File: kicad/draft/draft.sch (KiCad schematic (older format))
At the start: 22 parts, among them IC1 LP5024RSMR, J1 Conn_02x05_Odd_Even, U1 NodeMCU2

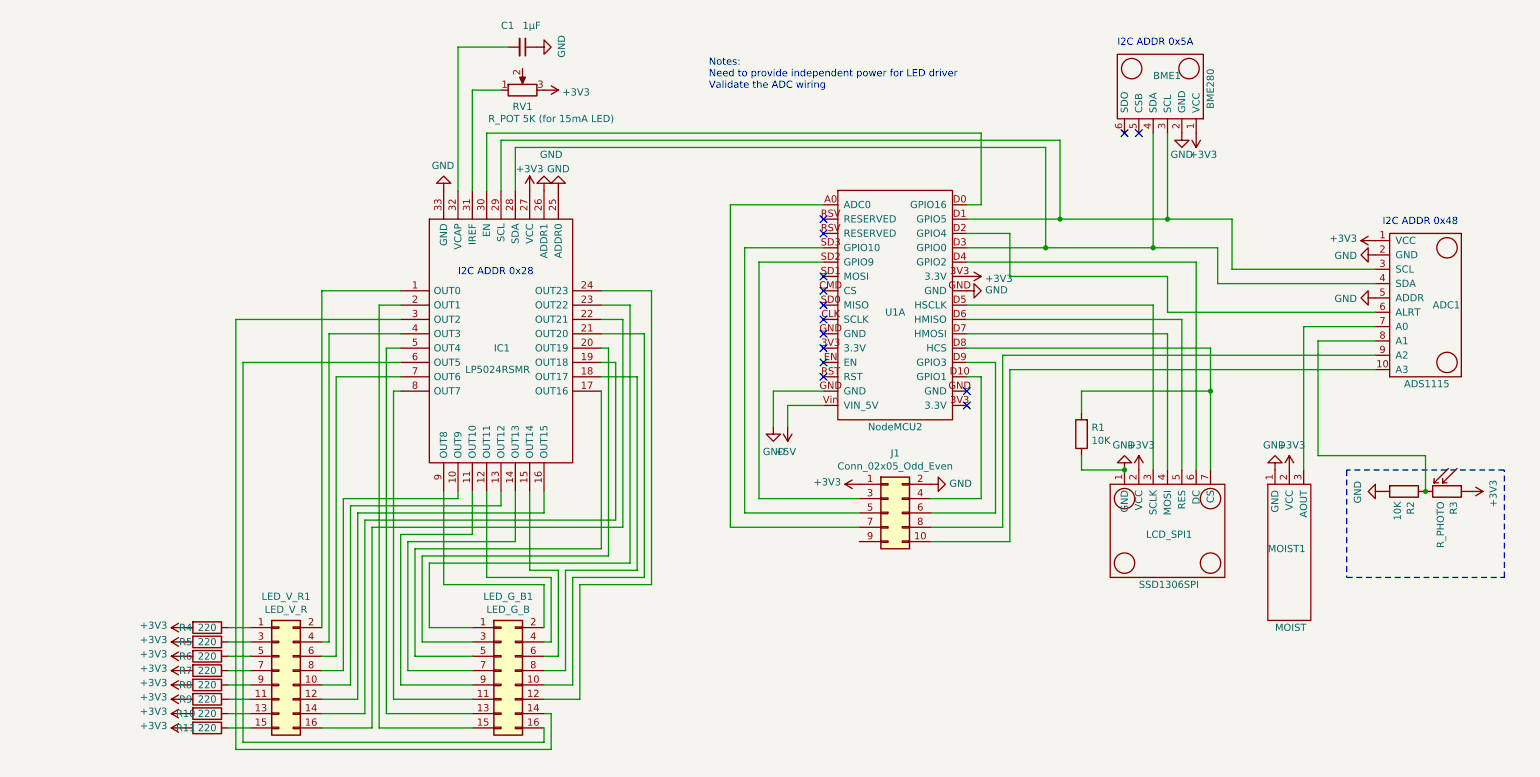
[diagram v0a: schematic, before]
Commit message: Added GND and 3V3 areas and tracks to connect NodeMCU
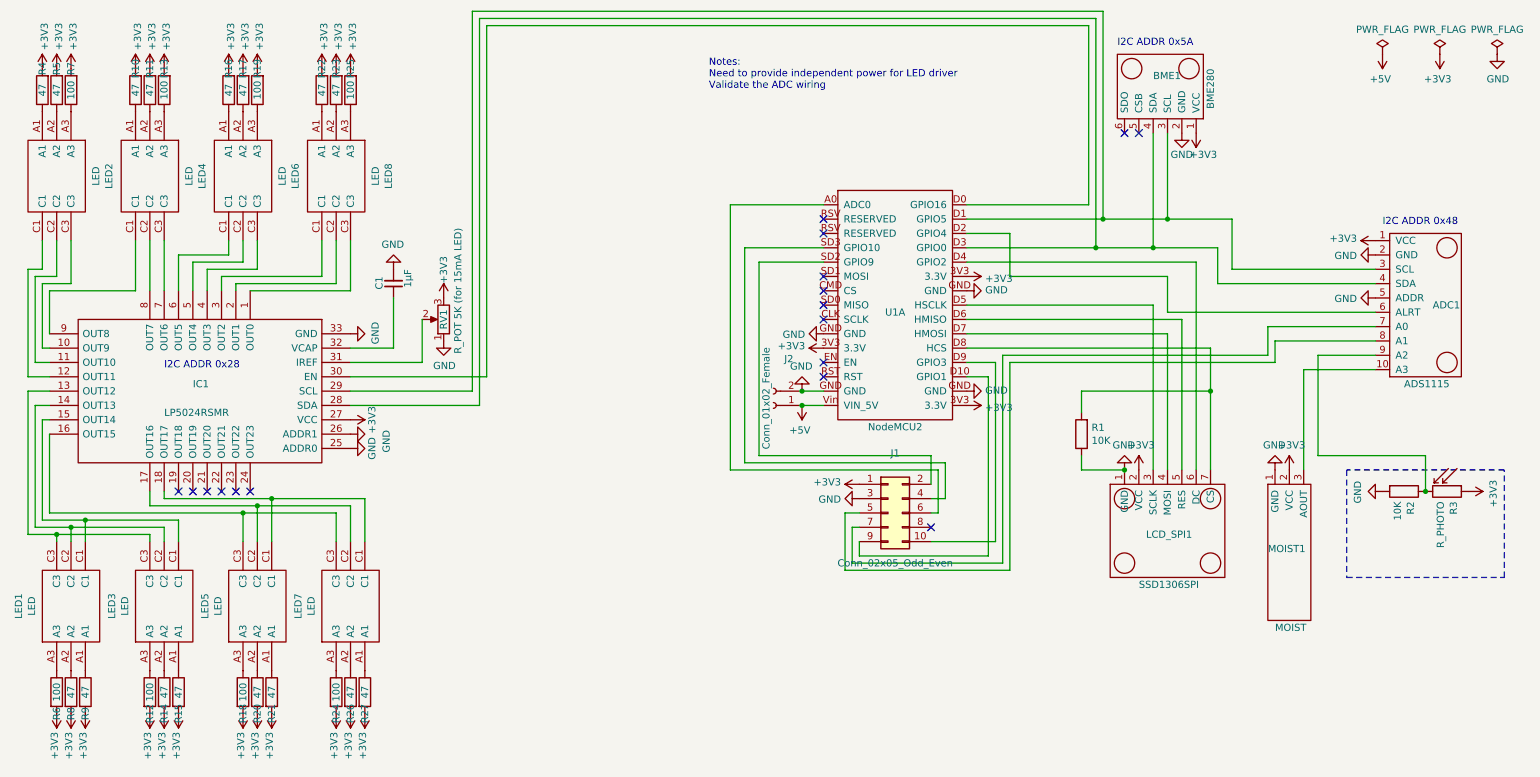
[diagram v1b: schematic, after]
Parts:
- removed LED_G_B1: LED_G_B, Connector_PinSocket_2.54mm:PinSocket_2x08_P2.54mm_Vertical, symbol Connector_Generic:Conn_02x08_Odd_Even
- removed LED_V_R1: LED_V_R, Connector_PinSocket_2.54mm:PinSocket_2x08_P2.54mm_Vertical, symbol Connector_Generic:Conn_02x08_Odd_Even
- added J2: Conn_01x02_Female, Connector_JST:JST_EH_S2B-EH_1x02_P2.50mm_Horizontal, symbol Connector:Conn_01x02_Female
- added LED1, LED2, LED3, LED4, LED5, LED6, LED7, LED8: LED, SamacSys:KRTBLSLPS132VUVXEQBTBVD8TWTZL1B, symbol SamaSys:KRTBLSLPS1.32-VUVX-EQ+BTBV-D8+TWTZ-L1-B
- added R12, R13, R18, R19, R24, R25: 100, Resistor_SMD:R_1206_3216Metric_Pad1.42x1.75mm_HandSolder, symbol Device:R
- added R14, R15, R16, R17, R20, R21, R22, R23, R26, R27: 47, Resistor_SMD:R_1206_3216Metric_Pad1.42x1.75mm_HandSolder, symbol Device:R
- R10, R11, R4, R5, R8, R9: value 220 -> 47; footprint Resistor_THT:R_Axial_DIN0207_L6.3mm_D2.5mm_P7.62mm_Horizontal -> Resistor_SMD:R_1206_3216Metric_Pad1.42x1.75mm_HandSolder
- R6, R7: value 220 -> 100; footprint Resistor_THT:R_Axial_DIN0207_L6.3mm_D2.5mm_P7.62mm_Horizontal -> Resistor_SMD:R_1206_3216Metric_Pad1.42x1.75mm_HandSolder
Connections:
- net +3V3: now also R12.2, R13.2, R14.2, R15.2, R16.2, R17.2, R18.2, R19.2, R20.2, R21.2, R22.2, R23.2, R24.2, R25.2, R26.2, R27.2
- net +5V: now also J2.1 (Pin_1)
- net GND: now also C1.2, J1.3 (Pin_3), RV1.1, J2.2 (Pin_2); no longer C1.1, J1.2 (Pin_2)
- net at U1.A0 (ADC0): now also J1.6 (Pin_6); no longer J1.7 (Pin_7)
- net at U1.D10 (GPIO1): now also J1.9 (Pin_9); no longer J1.4 (Pin_4)
- net at U1.D9 (GPIO3): now also J1.10 (Pin_10); no longer J1.6 (Pin_6)
- net at U1.SD2 (GPIO9): now also J1.2 (Pin_2); no longer J1.3 (Pin_3)
- net at U1.SD3 (GPIO10): now also J1.4 (Pin_4); no longer J1.5 (Pin_5)
- net at ADC1.10 (A3): now also MOIST1.3 (AOUT); no longer J1.10 (Pin_10)
- net at ADC1.7 (A0): now also J1.7 (Pin_7); no longer MOIST1.3 (AOUT)
- net at R2.1, R3.2: now also ADC1.9 (A2); no longer ADC1.8 (A1)
- net at J1.8 (Pin_8): no longer ADC1.9 (A2)
- net at IC1.32 (VCAP): now also C1.1; no longer C1.2
- net at IC1.8 (OUT7): now also LED4.C2
- net at IC1.5 (OUT4): now also LED6.C2
- net at IC1.3 (OUT2): now also LED8.C1
- net at IC1.2 (OUT1): now also LED8.C2
- net at IC1.6 (OUT5): now also LED6.C1
- net at IC1.9 (OUT8): now also LED4.C1
- net at IC1.12 (OUT11): now also LED2.C1
- net at IC1.17 (OUT16): now also LED5.C2, LED7.C2
- net at IC1.15 (OUT14): now also LED1.C1, LED3.C1
- net at IC1.14 (OUT13): now also LED1.C2, LED3.C2
- net at IC1.18 (OUT17): now also LED5.C1, LED7.C1
- net at IC1.11 (OUT10): now also LED2.C2
- net at R4.1: now also LED2.A1
- net at IC1.1 (OUT0): now also LED8.C3
- net at IC1.10 (OUT9): now also LED2.C3
- net at IC1.13 (OUT12): now also LED1.C3, LED3.C3
- net at IC1.16 (OUT15): now also LED5.C3, LED7.C3
- net at IC1.31 (IREF): now also RV1.2; no longer RV1.1
- net at IC1.4 (OUT3): now also LED6.C3
- net at IC1.7 (OUT6): now also LED4.C3
- net at R9.1: now also LED1.A1
- net at R10.1: now also LED4.A1
- net at R11.1: now also LED4.A2
- net at R5.1: now also LED2.A2
- net at R6.1: now also LED1.A3
- net at R7.1: now also LED2.A3
- net at R8.1: now also LED1.A2
- new net: ADC1.8 (A1), J1.5 (Pin_5)
- new net: LED8.A3, R25.1
- new net: LED8.A2, R23.1
- new net: LED8.A1, R22.1
- new net: LED6.A1, R16.1
- new net: LED6.A2, R17.1
- new net: LED6.A3, R19.1
- new net: LED4.A3, R13.1
- new net: LED3.A1, R15.1
- new net: LED3.A2, R14.1
- new net: LED3.A3, R12.1
- new net: LED5.A1, R21.1
- new net: LED5.A2, R20.1
- new net: LED5.A3, R18.1
- new net: LED7.A1, R27.1
- new net: LED7.A2, R26.1
- new net: LED7.A3, R24.1
- no-connect marks 14 -> 17
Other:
- moved on the sheet: C1, RV1

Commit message: PCB 0.1 sent to production
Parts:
- added C2: 1μF, Capacitor_SMD:C_1206_3216Metric_Pad1.42x1.75mm_HandSolder, symbol Device:C_Small
- C1: footprint Capacitor_THT:C_Disc_D5.1mm_W3.2mm_P5.00mm -> Capacitor_SMD:C_1206_3216Metric_Pad1.42x1.75mm_HandSolder
- R1, R2: footprint Resistor_THT:R_Axial_DIN0207_L6.3mm_D2.5mm_P7.62mm_Horizontal -> Resistor_SMD:R_1206_3216Metric_Pad1.42x1.75mm_HandSolder
- renumbered R3 to PHOTO1
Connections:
- net +3V3: now also C2.2
- net GND: now also C2.1
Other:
- moved on the sheet: C1, RV1
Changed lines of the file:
@@
 $EndComp
 $Comp
-L Device:R_PHOTO R3
+L Device:R_PHOTO PHOTO1
 U 1 1 5EEB65E3
 P 10500 3900
-F 0 "R3" H 10570 3946 50  0000 L CNN
+F 0 "PHOTO1" H 10570 3946 50  0000 L CNN
 F 1 "R_PHOTO" H 10570 3855 50  0000 L CNN
 F 2 "Connector_PinSocket_2.54mm:PinSocket_1x02_P2.54mm_Vertical" V 10550 3650 50  0001 L CNN
@@
 	-1   0    0    1
 $EndComp
-$Comp
-L power:+3V3 #PWR05
-U 1 1 5F023C2D
-P 7150 2400
-F 0 "#PWR05" H 7150 2250 50  0001 C CNN
-F 1 "+3V3" V 7165 2528 50  0000 L CNN
-F 2 "" H 7150 2400 50  0001 C CNN
-F 3 "" H 7150 2400 50  0001 C CNN
-	1    7150 2400
-	0    1    1    0
-$EndComp
-$Comp
-L power:GND #PWR06
-U 1 1 5F025492
-P 7150 2500
-F 0 "#PWR06" H 7150 2250 50  0001 C CNN
-F 1 "GND" V 7155 2372 50  0000 R CNN
-F 2 "" H 7150 2500 50  0001 C CNN
-F 3 "" H 7150 2500 50  0001 C CNN
-	1    7150 2500
-	0    -1   -1   0
-$EndComp
 NoConn ~ 8350 1400
 NoConn ~ 8250 1400
@@
 F 0 "R2" H 10270 3946 50  0000 L CNN
 F 1 "10K" H 10270 3855 50  0000 L CNN
-F 2 "Resistor_THT:R_Axial_DIN0207_L6.3mm_D2.5mm_P7.62mm_Horizontal" V 10130 3900 50  0001 C CNN
+F 2 "Resistor_SMD:R_1206_3216Metric_Pad1.42x1.75mm_HandSolder" V 10130 3900 50  0001 C CNN
 F 3 "~" H 10200 3900 50  0001 C CNN
 	1    10200 3900
@@
 F 0 "R1" H 7880 3454 50  0000 R CNN
 F 1 "10K" H 7880 3545 50  0000 R CNN
-F 2 "Resistor_THT:R_Axial_DIN0207_L6.3mm_D2.5mm_P7.62mm_Horizontal" V 7880 3500 50  0001 C CNN
+F 2 "Resistor_SMD:R_1206_3216Metric_Pad1.42x1.75mm_HandSolder" V 7880 3500 50  0001 C CNN
 F 3 "~" H 7950 3500 50  0001 C CNN
 	1    7950 3500
@@
 L power:GND #PWR0107
 U 1 1 5F6AA489
-P 2850 2800
-F 0 "#PWR0107" H 2850 2550 50  0001 C CNN
-F 1 "GND" H 2855 2627 50  0000 C CNN
-F 2 "" H 2850 2800 50  0001 C CNN
-F 3 "" H 2850 2800 50  0001 C CNN
-	1    2850 2800
-	0    -1   -1   0
+P 3400 2350
+F 0 "#PWR0107" H 3400 2100 50  0001 C CNN
+F 1 "GND" H 3405 2177 50  0000 C CNN
+F 2 "" H 3400 2350 50  0001 C CNN
+F 3 "" H 3400 2350 50  0001 C CNN
+	1    3400 2350
+	-1   0    0    1
 $EndComp
 Text Notes 5350 1100 0    50   ~ 0
@@
 L power:+3V3 #PWR0103
 U 1 1 5F508F6C
-P 2850 3400
-F 0 "#PWR0103" H 2850 3250 50  0001 C CNN
-F 1 "+3V3" H 2850 3550 50  0000 C CNN
-F 2 "" H 2850 3400 50  0001 C CNN
-F 3 "" H 2850 3400 50  0001 C CNN
-	1    2850 3400
+P 3500 3400
+F 0 "#PWR0103" H 3500 3250 50  0001 C CNN
+F 1 "+3V3" H 3500 3550 50  0000 C CNN
+F 2 "" H 3500 3400 50  0001 C CNN
+F 3 "" H 3500 3400 50  0001 C CNN
+	1    3500 3400
 	0    1    1    0
 $EndComp
@@
 L Device:R_POT RV1
 U 1 1 5FBB8D76
-P 3500 2700
-F 0 "RV1" V 3500 2700 50  0000 C CNN
-F 1 "R_POT 5K (for 15mA LED)" V 3400 2500 50  0000 C CNN
-F 2 "Potentiometer_THT:Potentiometer_Bourns_PTV09A-1_Single_Vertical" H 3500 2700 50  0001 C CNN
-F 3 "~" H 3500 2700 50  0001 C CNN
-	1    3500 2700
+P 3850 2700
+F 0 "RV1" V 3850 2700 50  0000 C CNN
+F 1 "R_POT 5K (for 15mA LED)" V 3750 2500 50  0000 C CNN
+F 2 "Potentiometer_THT:Potentiometer_Bourns_PTV09A-1_Single_Vertical" H 3850 2700 50  0001 C CNN
+F 3 "~" H 3850 2700 50  0001 C CNN
+	1    3850 2700
 	-1   0    0    1
 $EndComp
@@
 L power:+3V3 #PWR04
 U 1 1 5FAA6249
-P 3500 2550
-F 0 "#PWR04" H 3500 2400 50  0001 C CNN
-F 1 "+3V3" V 3500 2650 50  0000 L CNN
-F 2 "" H 3500 2550 50  0001 C CNN
-F 3 "" H 3500 2550 50  0001 C CNN
-	1    3500 2550
+P 3850 2550
+F 0 "#PWR04" H 3850 2400 50  0001 C CNN
+F 1 "+3V3" V 3850 2650 50  0000 L CNN
+F 2 "" H 3850 2550 50  0001 C CNN
+F 3 "" H 3850 2550 50  0001 C CNN
+	1    3850 2550
 	1    0    0    -1
 $EndComp
@@
 L power:GND #PWR0104
 U 1 1 5F518415
-P 3150 2350
-F 0 "#PWR0104" H 3150 2100 50  0001 C CNN
-F 1 "GND" H 3155 2177 50  0000 C CNN
-F 2 "" H 3150 2350 50  0001 C CNN
-F 3 "" H 3150 2350 50  0001 C CNN
-	1    3150 2350
+P 3600 2350
+F 0 "#PWR0104" H 3600 2100 50  0001 C CNN
+F 1 "GND" H 3605 2177 50  0000 C CNN
+F 2 "" H 3600 2350 50  0001 C CNN
+F 3 "" H 3600 2350 50  0001 C CNN
+	1    3600 2350
 	-1   0    0    1
 $EndComp
@@
 L Device:C_Small C1
 U 1 1 5F50D4CF
-P 3150 2450
-F 0 "C1" V 3250 2400 50  0000 L CNN
-F 1 "1μF" V 3050 2350 50  0000 L CNN
-F 2 "Capacitor_THT:C_Disc_D5.1mm_W3.2mm_P5.00mm" H 3150 2450 50  0001 C CNN
-F 3 "~" H 3150 2450 50  0001 C CNN
-	1    3150 2450
-	-1   0    0    1
-$EndComp
-Wire Wire Line
-	3150 2550 3150 2900
-Wire Wire Line
-	2850 2900 3150 2900
-Wire Wire Line
-	3350 3000 2850 3000
-Wire Wire Line
-	2850 3200 3700 3200
-Wire Wire Line
-	2850 3300 3750 3300
+P 3600 2450
+F 0 "C1" V 3700 2400 50  0000 L CNN
+F 1 "1μF" V 3500 2350 50  0000 L CNN
+F 2 "Capacitor_SMD:C_1206_3216Metric_Pad1.42x1.75mm_HandSolder" H 3600 2450 50  0001 C CNN
+F 3 "~" H 3600 2450 50  0001 C CNN
+	1    3600 2450
+	-1   0    0    1
+$EndComp
+Wire Wire Line
+	3600 2550 3600 2900
+Wire Wire Line
+	2850 3200 3150 3200
+Wire Wire Line
+	2850 3300 3200 3300
 NoConn ~ 2150 3900
 NoConn ~ 2050 3900
@@
 	600  3200 600  4200
 Wire Wire Line
-	3700 3200 3700 550
-Wire Wire Line
-	3700 550  8100 550
+	3150 3200 3150 550
 Wire Wire Line
 	8100 550  8100 2000
@@
 	8100 2000 8550 2000
 Wire Wire Line
-	3750 3300 3750 600
-Wire Wire Line
-	3750 600  8050 600
+	3200 3300 3200 600
 Wire Wire Line
 	8050 600  8050 2200
@@
 Wire Wire Line
 	8050 2200 8450 2200
-Wire Wire Line
-	3800 3100 3800 650
-Wire Wire Line
-	3800 650  8000 650
 Wire Wire Line
 	8000 650  8000 1900
@@
 	6150 3300 6000 3300
 Wire Wire Line
-	2850 3100 3800 3100
-Wire Wire Line
-	3350 2700 3350 3000
+	2850 3100 3250 3100
 $Comp
 L power:GND #PWR0135
 U 1 1 612E9063
-P 3500 2850
-F 0 "#PWR0135" H 3500 2600 50  0001 C CNN
-F 1 "GND" H 3505 2677 50  0000 C CNN
-F 2 "" H 3500 2850 50  0001 C CNN
-F 3 "" H 3500 2850 50  0001 C CNN
-	1    3500 2850
-	1    0    0    -1
-$EndComp
-$Comp
-L power:GND #PWR0136
-U 1 1 61312598
-P 6150 2800
-F 0 "#PWR0136" H 6150 2550 50  0001 C CNN
-F 1 "GND" V 6155 2672 50  0000 R CNN
-F 2 "" H 6150 2800 50  0001 C CNN
-F 3 "" H 6150 2800 50  0001 C CNN
-	1    6150 2800
-	0    1    1    0
-$EndComp
-$Comp
-L power:GND #PWR0137
-U 1 1 61313510
-P 7150 3200
-F 0 "#PWR0137" H 7150 2950 50  0001 C CNN
-F 1 "GND" V 7155 3072 50  0000 R CNN
-F 2 "" H 7150 3200 50  0001 C CNN
-F 3 "" H 7150 3200 50  0001 C CNN
-	1    7150 3200
-	0    -1   -1   0
+P 3850 2850
+F 0 "#PWR0135" H 3850 2600 50  0001 C CNN
+F 1 "GND" H 3855 2677 50  0000 C CNN
+F 2 "" H 3850 2850 50  0001 C CNN
+F 3 "" H 3850 2850 50  0001 C CNN
+	1    3850 2850
+	1    0    0    -1
 $EndComp
 Wire Wire Line
@@
 Wire Wire Line
 	6900 3950 7000 3950
-$Comp
-L power:+3V3 #PWR0138
-U 1 1 613375CB
-P 7150 3300
-F 0 "#PWR0138" H 7150 3150 50  0001 C CNN
-F 1 "+3V3" V 7165 3428 50  0000 L CNN
-F 2 "" H 7150 3300 50  0001 C CNN
-F 3 "" H 7150 3300 50  0001 C CNN
-	1    7150 3300
-	0    1    1    0
-$EndComp
-$Comp
-L power:+3V3 #PWR0139
-U 1 1 61338424
-P 6150 2900
-F 0 "#PWR0139" H 6150 2750 50  0001 C CNN
-F 1 "+3V3" V 6165 3028 50  0000 L CNN
-F 2 "" H 6150 2900 50  0001 C CNN
-F 3 "" H 6150 2900 50  0001 C CNN
-	1    6150 2900
-	0    -1   -1   0
-$EndComp
 $Comp
 L power:GND #PWR0140
@@
 Wire Wire Line
 	7450 3000 7450 4450
+Wire Wire Line
+	3400 2800 3400 2350
+Wire Wire Line
+	2850 2800 3400 2800
+Wire Wire Line
+	3250 650  3250 3100
+Wire Wire Line
+	2850 2900 3600 2900
+Wire Wire Line
+	2850 3000 3700 3000
+Wire Wire Line
+	3700 2700 3700 3000
+Wire Wire Line
+	2850 3400 3400 3400
+$Comp
+L Device:C_Small C2
+U 1 1 6184C4BB
+P 3400 3300
+F 0 "C2" H 3492 3346 50  0000 L CNN
+F 1 "1μF" H 3492 3255 50  0000 L CNN
+F 2 "Capacitor_SMD:C_1206_3216Metric_Pad1.42x1.75mm_HandSolder" H 3400 3300 50  0001 C CNN
+F 3 "~" H 3400 3300 50  0001 C CNN
+	1    3400 3300
+	1    0    0    -1
+$EndComp
+Connection ~ 3400 3400
+Wire Wire Line
+	3400 3400 3500 3400
+Wire Wire Line
+	3400 2800 3400 3200
+Connection ~ 3400 2800
+Wire Wire Line
+	3250 650  8000 650
+Wire Wire Line
+	3200 600  8050 600
+Wire Wire Line
+	3150 550  8100 550
+$Comp
+L power:+3V3 #PWR0136
+U 1 1 61ACAD33
+P 6150 2900
+F 0 "#PWR0136" H 6150 2750 50  0001 C CNN
+F 1 "+3V3" V 6165 3028 50  0000 L CNN
+F 2 "" H 6150 2900 50  0001 C CNN
+F 3 "" H 6150 2900 50  0001 C CNN
+	1    6150 2900
+	0    -1   -1   0
+$EndComp
+$Comp
+L power:+3V3 #PWR0137
+U 1 1 61AD11DA
+P 7150 2400
+F 0 "#PWR0137" H 7150 2250 50  0001 C CNN
+F 1 "+3V3" V 7165 2528 50  0000 L CNN
+F 2 "" H 7150 2400 50  0001 C CNN
+F 3 "" H 7150 2400 50  0001 C CNN
+	1    7150 2400
+	0    1    1    0
+$EndComp
+$Comp
+L power:+3V3 #PWR0138
+U 1 1 61AD27FC
+P 7150 3300
+F 0 "#PWR0138" H 7150 3150 50  0001 C CNN
+F 1 "+3V3" V 7165 3428 50  0000 L CNN
+F 2 "" H 7150 3300 50  0001 C CNN
+F 3 "" H 7150 3300 50  0001 C CNN
+	1    7150 3300
+	0    1    1    0
+$EndComp
+$Comp
+L power:GND #PWR0139
+U 1 1 61AE1CBB
+P 7150 2500
+F 0 "#PWR0139" H 7150 2250 50  0001 C CNN
+F 1 "GND" V 7155 2372 50  0000 R CNN
+F 2 "" H 7150 2500 50  0001 C CNN
+F 3 "" H 7150 2500 50  0001 C CNN
+	1    7150 2500
+	0    -1   -1   0
+$EndComp
+$Comp
+L power:GND #PWR0143
+U 1 1 61AE2A28
+P 7150 3200
+F 0 "#PWR0143" H 7150 2950 50  0001 C CNN
+F 1 "GND" V 7155 3072 50  0000 R CNN
+F 2 "" H 7150 3200 50  0001 C CNN
+F 3 "" H 7150 3200 50  0001 C CNN
+	1    7150 3200
+	0    -1   -1   0
+$EndComp
+$Comp
+L power:GND #PWR0144
+U 1 1 61AE32D0
+P 6150 2800
+F 0 "#PWR0144" H 6150 2550 50  0001 C CNN
+F 1 "GND" V 6155 2672 50  0000 R CNN
+F 2 "" H 6150 2800 50  0001 C CNN
+F 3 "" H 6150 2800 50  0001 C CNN
+	1    6150 2800
+	0    1    1    0
+$EndComp
 $EndSCHEMATC
